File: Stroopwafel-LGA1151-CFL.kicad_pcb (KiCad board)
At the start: 2 copper layers, 84 parts, among them J1 PCIe_x16_CPU, J2 DP_A, J3 DP_B, J4 DP_C, Q1 2N7002, Q2 2N7002, Q3 2N7002, Q4 2N7002, Q5 2N7002, Q6 2N7002

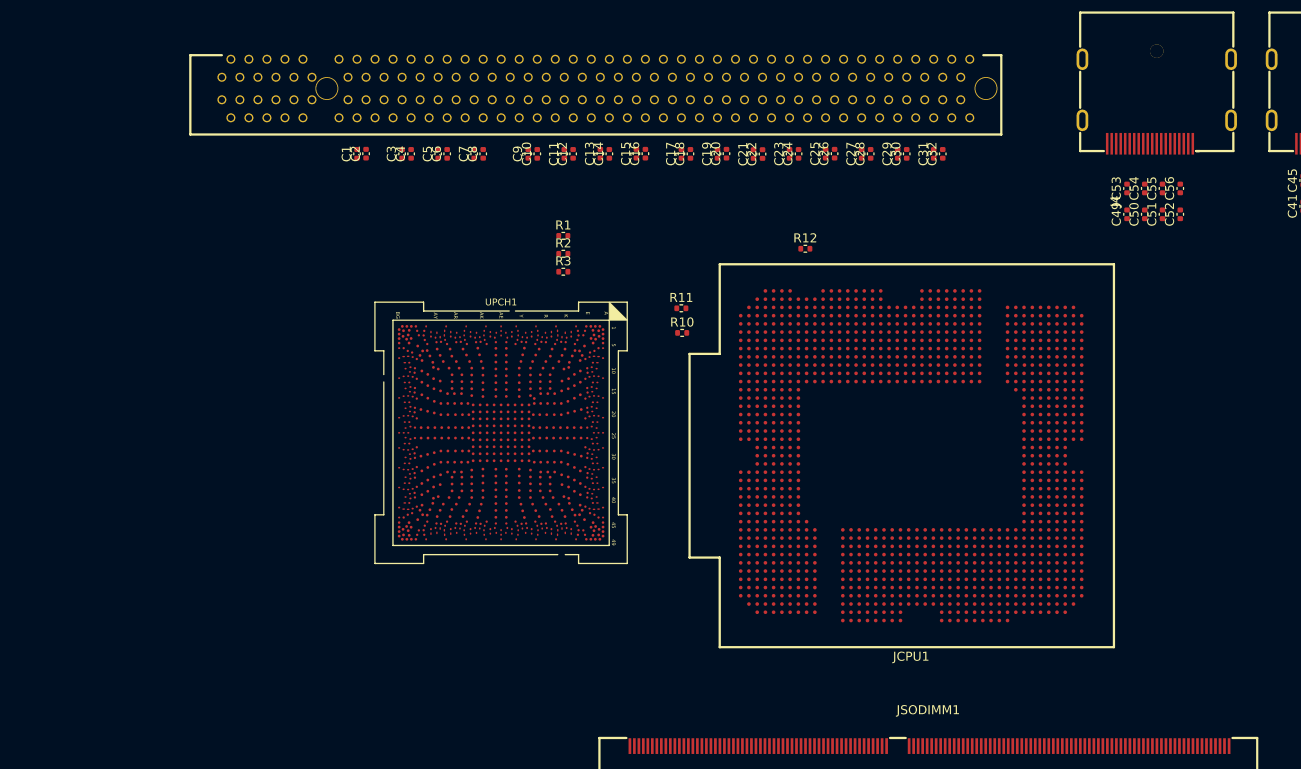
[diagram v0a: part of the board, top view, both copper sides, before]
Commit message: Added LGA1151 socket bracket holes
stolen from another lga1151 footprint that has wrong pin numbers....
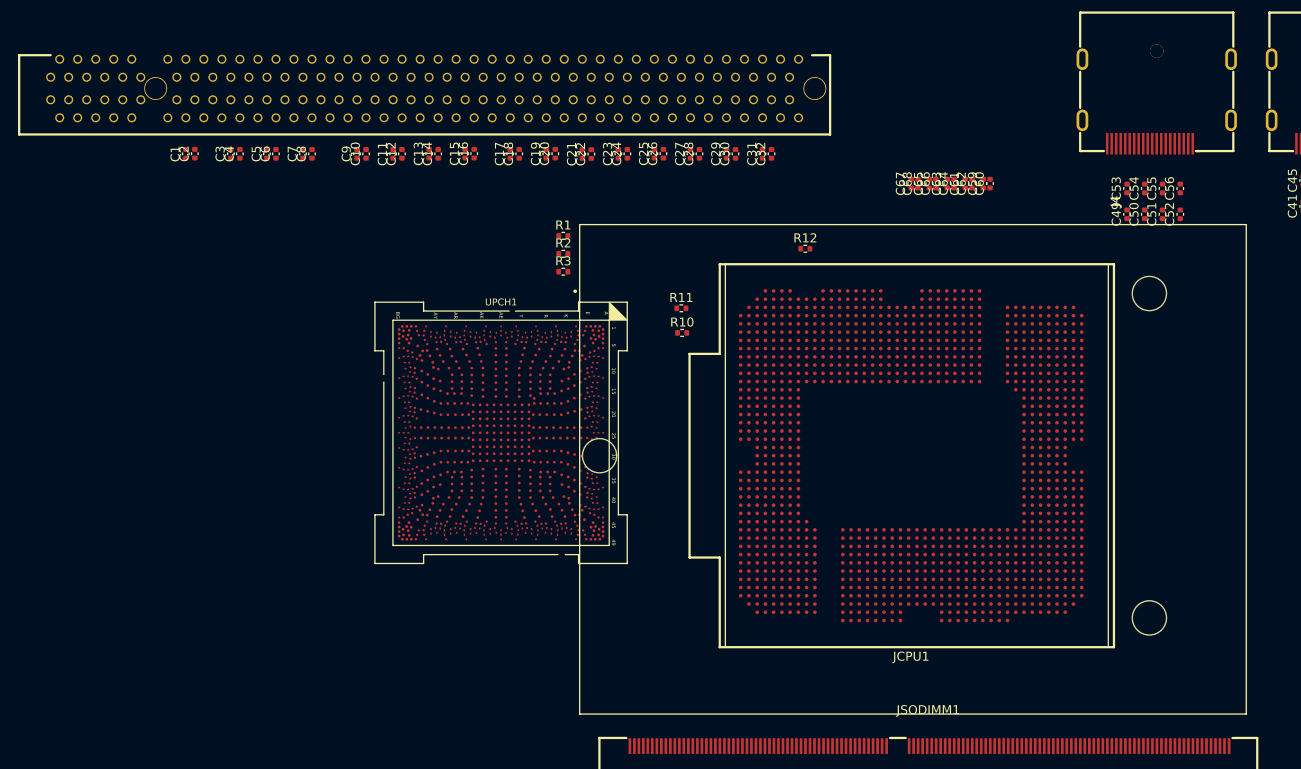
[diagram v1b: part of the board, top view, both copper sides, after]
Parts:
- added C59: 0.1uF, Capacitor_SMD:C_0402_1005Metric, F.Cu at (208.0, 39.8)
- added C60: 0.1uF, Capacitor_SMD:C_0402_1005Metric, F.Cu at (208.8, 39.8)
- added C61: 0.1uF, Capacitor_SMD:C_0402_1005Metric, F.Cu at (206.0, 39.8)
- added C62: 0.1uF, Capacitor_SMD:C_0402_1005Metric, F.Cu at (206.8, 39.8)
- added C63: 0.1uF, Capacitor_SMD:C_0402_1005Metric, F.Cu at (204.0, 39.8)
- added C64: 0.1uF, Capacitor_SMD:C_0402_1005Metric, F.Cu at (204.8, 39.8)
- added C65: 0.1uF, Capacitor_SMD:C_0402_1005Metric, F.Cu at (202.0, 39.8)
- added C66: 0.1uF, Capacitor_SMD:C_0402_1005Metric, F.Cu at (202.8, 39.8)
- added C67: 0.1uF, Capacitor_SMD:C_0402_1005Metric, F.Cu at (200.0, 39.8)
- added C68: 0.1uF, Capacitor_SMD:C_0402_1005Metric, F.Cu at (200.8, 39.8)
- moved C1 19.0 mm to (119.5, 36.5)
- moved C10 19.0 mm to (139.5, 36.5)
- moved C11 19.0 mm to (142.5, 36.5)
- moved C12 19.0 mm to (143.5, 36.5)
- moved C13 19.0 mm to (146.5, 36.5)
- moved C14 19.0 mm to (147.5, 36.5)
- moved C15 19.0 mm to (150.5, 36.5)
- moved C16 19.0 mm to (151.5, 36.5)
- moved C17 19.0 mm to (155.5, 36.5)
- moved C18 19.0 mm to (156.5, 36.5)
- moved C19 19.0 mm to (159.5, 36.5)
- moved C2 19.0 mm to (120.5, 36.5)
- moved C20 19.0 mm to (160.5, 36.5)
- moved C21 19.0 mm to (163.5, 36.5)
- moved C22 19.0 mm to (164.5, 36.5)
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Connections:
- J2 pad 19: unconnected-(J2-DP_PWR_RETURN-Pad19) -> GND
- J3 pad 19: unconnected-(J3-DP_PWR_RETURN-Pad19) -> GND
- J4 pad 19: unconnected-(J4-DP_PWR_RETURN-Pad19) -> GND
- JCPU1 pad C9: unconnected-(JCPU1D-EDP_TXN_1-PadC9) -> iGPU_eDP_TX1-
- JCPU1 pad D10: unconnected-(JCPU1D-EDP_TXN_0-PadD10) -> iGPU_eDP_TX0-
- JCPU1 pad D12: unconnected-(JCPU1D-EDP_AUXP-PadD12) -> iGPU_eDP_AUX+
- JCPU1 pad D9: unconnected-(JCPU1D-EDP_TXP_1-PadD9) -> iGPU_eDP_TX1+
- JCPU1 pad E10: unconnected-(JCPU1D-EDP_TXP_0-PadE10) -> iGPU_eDP_TX0+
- JCPU1 pad E12: unconnected-(JCPU1D-EDP_AUXN-PadE12) -> iGPU_eDP_AUX-
- JCPU1 pad F9: unconnected-(JCPU1D-EDP_TXN_3-PadF9) -> iGPU_eDP_TX3-
- JCPU1 pad G10: unconnected-(JCPU1D-EDP_TXN_2-PadG10) -> iGPU_eDP_TX2-
- JCPU1 pad G9: unconnected-(JCPU1D-EDP_TXP_3-PadG9) -> iGPU_eDP_TX3+
- JCPU1 pad H10: unconnected-(JCPU1D-EDP_TXP_2-PadH10) -> iGPU_eDP_TX2+
- UPCH1 pad AU48: unconnected-(UPCH1C-GPP_F21/EDP_BKLTCTL-PadAU48) -> eDP_PWM
- UPCH1 pad AV44: unconnected-(UPCH1C-GPP_F19/EDP_VDDEN-PadAV44) -> eDP_VDDEN
- UPCH1 pad AV46: unconnected-(UPCH1C-GPP_F20/EDP_BKLTEN-PadAV46) -> eDP_BLEN

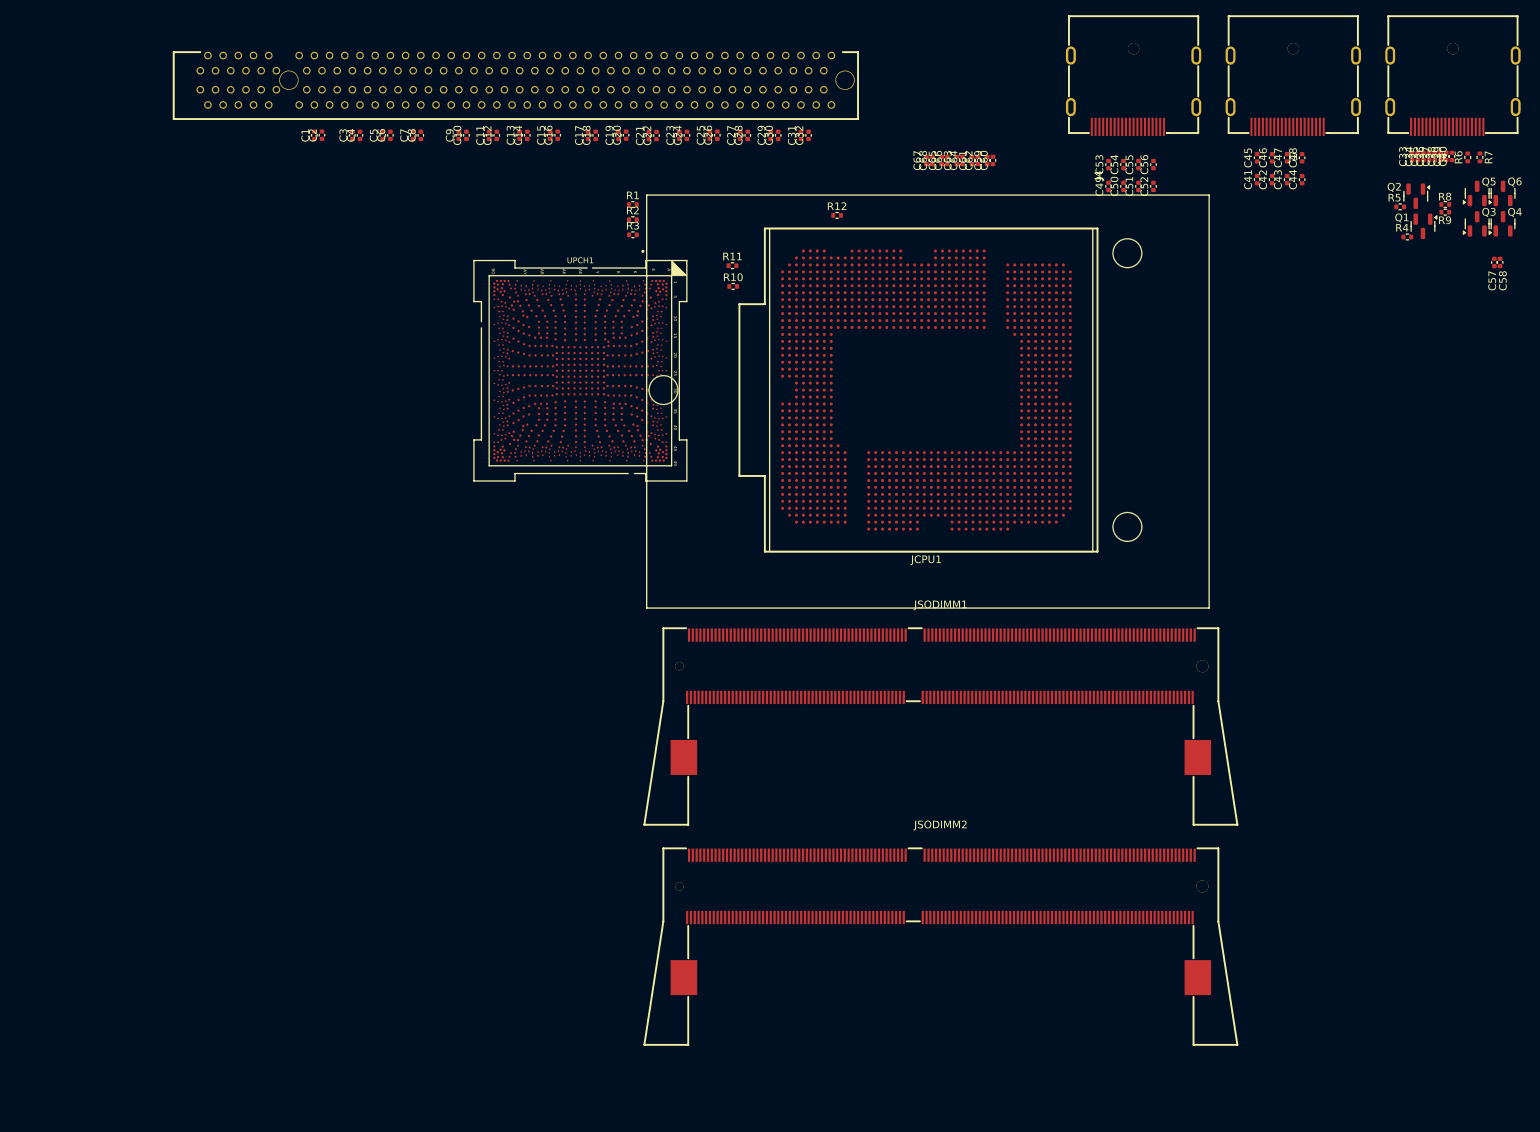
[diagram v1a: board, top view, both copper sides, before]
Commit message: Added CPU CFG resistors
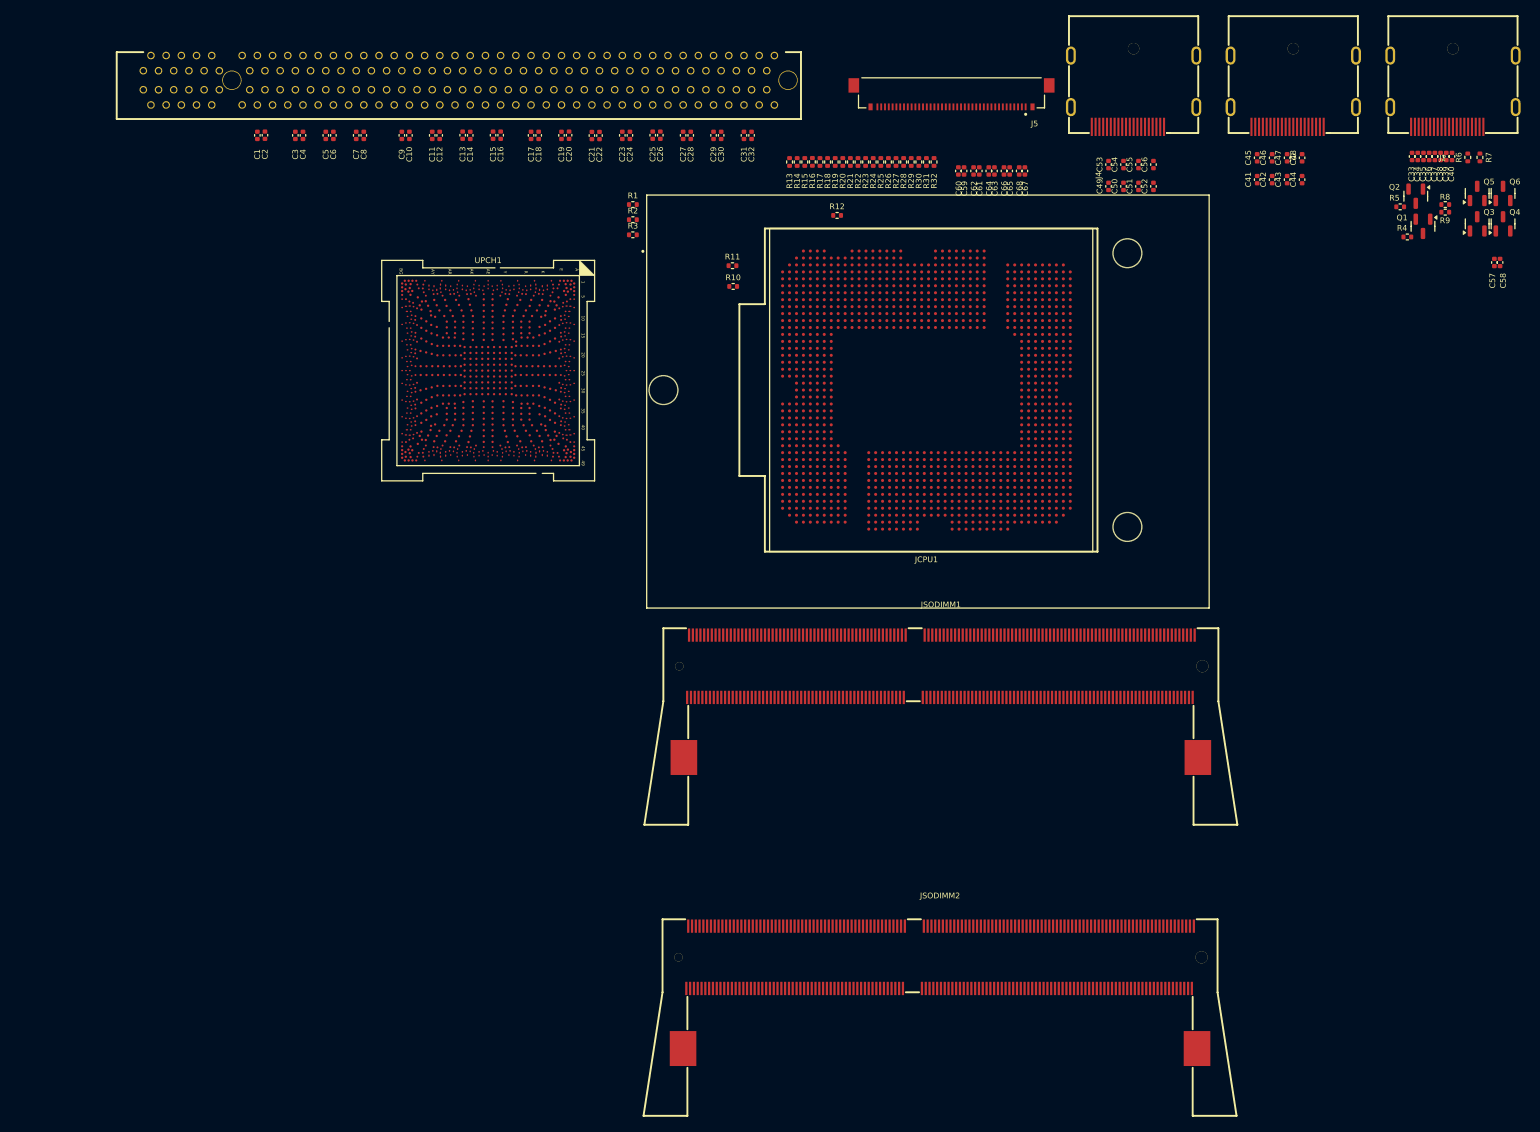
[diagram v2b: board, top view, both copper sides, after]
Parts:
- added J5: eDP 4-lane 40-pin ipex, A-my-stuff:40pIPEX_20455-040E-76, F.Cu at (203.3, 30.8)
- added R13: 1kΩ, Resistor_SMD:R_0402_1005Metric, F.Cu at (182.0, 40.0)
- added R14: 1kΩ, Resistor_SMD:R_0402_1005Metric, F.Cu at (183.0, 40.0)
- added R15: 1kΩ, Resistor_SMD:R_0402_1005Metric, F.Cu at (184.0, 40.0)
- added R16: 1kΩ, Resistor_SMD:R_0402_1005Metric, F.Cu at (185.0, 40.0)
- added R17: 1kΩ, Resistor_SMD:R_0402_1005Metric, F.Cu at (186.0, 40.0)
- added R18: 1kΩ, Resistor_SMD:R_0402_1005Metric, F.Cu at (187.0, 40.0)
- added R19: 1kΩ, Resistor_SMD:R_0402_1005Metric, F.Cu at (188.0, 40.0)
- added R20: 1kΩ, Resistor_SMD:R_0402_1005Metric, F.Cu at (189.0, 40.0)
- added R21: 1kΩ, Resistor_SMD:R_0402_1005Metric, F.Cu at (190.0, 40.0)
- added R22: 1kΩ, Resistor_SMD:R_0402_1005Metric, F.Cu at (191.0, 40.0)
- added R23: 1kΩ, Resistor_SMD:R_0402_1005Metric, F.Cu at (192.0, 40.0)
- added R24: 1kΩ, Resistor_SMD:R_0402_1005Metric, F.Cu at (193.0, 40.0)
- added R25: 1kΩ, Resistor_SMD:R_0402_1005Metric, F.Cu at (194.0, 40.0)
- added R26: 1kΩ, Resistor_SMD:R_0402_1005Metric, F.Cu at (195.0, 40.0)
- added R27: 1kΩ, Resistor_SMD:R_0402_1005Metric, F.Cu at (196.0, 40.0)
- added R28: 1kΩ, Resistor_SMD:R_0402_1005Metric, F.Cu at (197.0, 40.0)
- added R29: 1kΩ, Resistor_SMD:R_0402_1005Metric, F.Cu at (198.0, 40.0)
- added R30: 1kΩ, Resistor_SMD:R_0402_1005Metric, F.Cu at (199.0, 40.0)
- added R31: 1kΩ, Resistor_SMD:R_0402_1005Metric, F.Cu at (200.0, 40.0)
- added R32: 1kΩ, Resistor_SMD:R_0402_1005Metric, F.Cu at (201.0, 40.0)
- moved C67 13.0 mm to (212.9, 41.2)
- moved UPCH1 12.1 mm to (142.4, 67.4)
- moved C68 11.5 mm to (212.2, 41.2)
- moved JSODIMM2 9.33 mm to (201.8, 148.6)
- moved C65 9.06 mm to (210.9, 41.2)
- moved C66 7.58 mm to (210.2, 41.2)
- moved C1 7.50 mm to (112.0, 36.5)
- moved C10 7.50 mm to (132.0, 36.5)
- moved C11 7.50 mm to (135.0, 36.5)
- moved C12 7.50 mm to (136.0, 36.5)
- moved C13 7.50 mm to (139.0, 36.5)
- moved C14 7.50 mm to (140.0, 36.5)
- moved C15 7.50 mm to (143.0, 36.5)
- moved C16 7.50 mm to (144.0, 36.5)
- moved C17 7.50 mm to (148.0, 36.5)
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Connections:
- JCPU1 pad E14: unconnected-(JCPU1E-CFG_16-PadE14) -> Net-(JCPU1E-CFG_16)
- JCPU1 pad E16: unconnected-(JCPU1E-CFG_9-PadE16) -> Net-(JCPU1E-CFG_9)
- JCPU1 pad F14: unconnected-(JCPU1E-CFG_17-PadF14) -> Net-(JCPU1E-CFG_17)
- JCPU1 pad F15: unconnected-(JCPU1E-CFG_1-PadF15) -> Net-(JCPU1E-CFG_1)
- JCPU1 pad F16: unconnected-(JCPU1E-CFG_2-PadF16) -> Net-(JCPU1E-CFG_2)
- JCPU1 pad F17: unconnected-(JCPU1E-CFG_10-PadF17) -> Net-(JCPU1E-CFG_10)
- JCPU1 pad F18: unconnected-(JCPU1E-CFG_19-PadF18) -> Net-(JCPU1E-CFG_19)
- JCPU1 pad F19: unconnected-(JCPU1E-CFG_4-PadF19) -> Net-(JCPU1E-CFG_4)
- JCPU1 pad F20: unconnected-(JCPU1E-CFG_13-PadF20) -> Net-(JCPU1E-CFG_13)
- JCPU1 pad F21: unconnected-(JCPU1E-CFG_14-PadF21) -> Net-(JCPU1E-CFG_14)
- JCPU1 pad G16: unconnected-(JCPU1E-CFG_8-PadG16) -> Net-(JCPU1E-CFG_8)
- JCPU1 pad G18: unconnected-(JCPU1E-CFG_18-PadG18) -> Net-(JCPU1E-CFG_18)
- JCPU1 pad G20: unconnected-(JCPU1E-CFG_12-PadG20) -> Net-(JCPU1E-CFG_12)
- JCPU1 pad G21: unconnected-(JCPU1E-CFG_6-PadG21) -> Net-(JCPU1E-CFG_6)
- JCPU1 pad H15: unconnected-(JCPU1E-CFG_0-PadH15) -> Net-(JCPU1E-CFG_0)
- JCPU1 pad H16: unconnected-(JCPU1E-CFG_3-PadH16) -> Net-(JCPU1E-CFG_3)
- JCPU1 pad H17: unconnected-(JCPU1E-CFG_11-PadH17) -> Net-(JCPU1E-CFG_11)
- JCPU1 pad H18: unconnected-(JCPU1E-CFG_5-PadH18) -> Net-(JCPU1E-CFG_5)
- JCPU1 pad H19: unconnected-(JCPU1E-CFG_15-PadH19) -> Net-(JCPU1E-CFG_15)
- JCPU1 pad H20: unconnected-(JCPU1E-CFG_7-PadH20) -> Net-(JCPU1E-CFG_7)

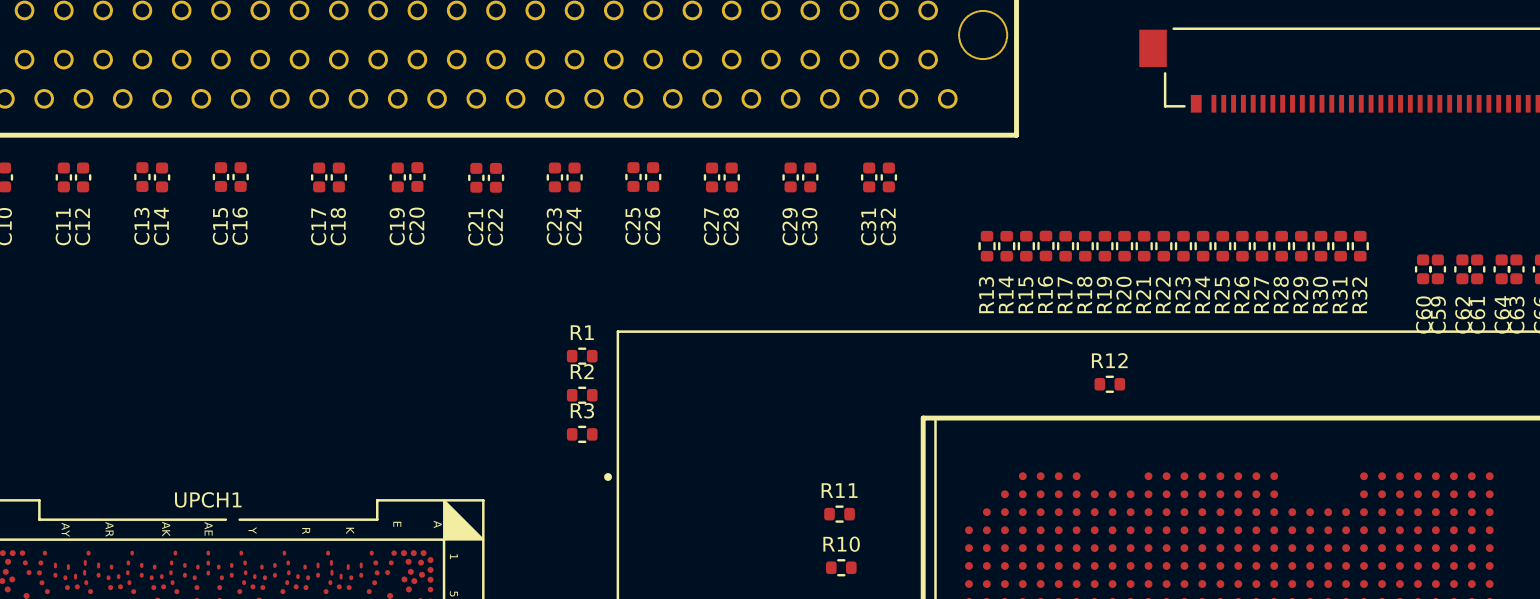
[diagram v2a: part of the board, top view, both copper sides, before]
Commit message: Added PCH PCIe rootport/bifurcation notes
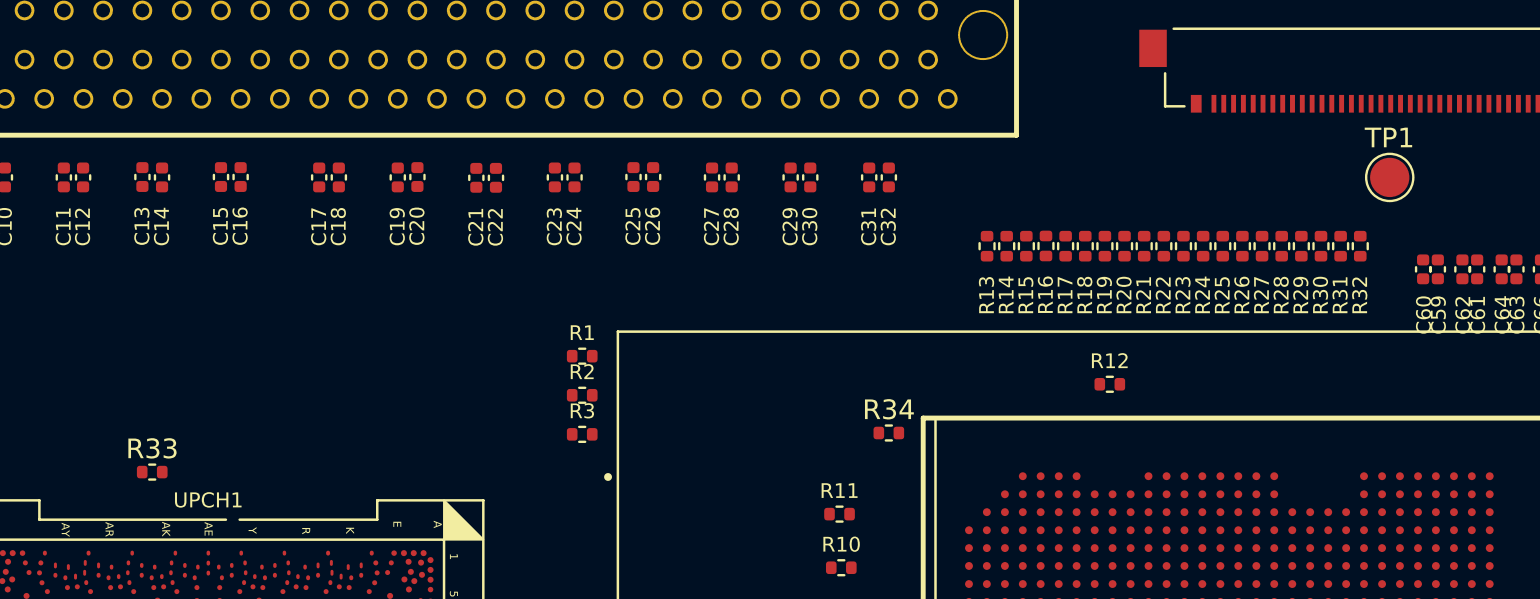
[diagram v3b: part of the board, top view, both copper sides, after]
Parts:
- added R33: 33.2Ω, Resistor_SMD:R_0402_1005Metric, F.Cu at (139.5, 51.5)
- added R34: 20Ω, Resistor_SMD:R_0402_1005Metric, F.Cu at (177.0, 49.5)
- added TP1: eDP-pwm-but-from-CPU?, TestPoint:TestPoint_Pad_D2.0mm, F.Cu at (202.5, 36.5)
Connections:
- JCPU1 pad B3: unconnected-(JCPU1J-PROC_TRIGOUT-PadB3) -> Net-(JCPU1J-PROC_TRIGOUT)
- JCPU1 pad D1: unconnected-(JCPU1J-PROC_TRIGIN-PadD1) -> TRIG_PCH_TO_CPU
- JCPU1 pad D14: unconnected-(JCPU1D-EDP_DISP_UTIL-PadD14) -> Net-(JCPU1D-EDP_DISP_UTIL)
- UPCH1 pad AK2: unconnected-(UPCH1J-TRIGGER_IN-PadAK2) -> TRIG_CPU_TO_PCH
- UPCH1 pad AK3: unconnected-(UPCH1J-TRIGGER_OUT-PadAK3) -> Net-(UPCH1J-TRIGGER_OUT)

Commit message: nooo they be stealin my stroopwafel
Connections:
- J5 pad 36: unconnected-(J5-BL_PWR-Pad36) -> Net-(J5-BL_PWR-Pad36)
- J5 pad 37: unconnected-(J5-BL_PWR-Pad37) -> Net-(J5-BL_PWR-Pad36)
- J5 pad 38: unconnected-(J5-BL_PWR-Pad38) -> Net-(J5-BL_PWR-Pad36)
- J5 pad 39: unconnected-(J5-BL_PWR-Pad39) -> Net-(J5-BL_PWR-Pad36)
